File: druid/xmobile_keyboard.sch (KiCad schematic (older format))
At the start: 22 parts

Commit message: Added microSD slot.
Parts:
- removed R?: 10kOmh, Resistors_SMD:R_0603_HandSoldering, symbol R-RESCUE-xmobile
- added >0.1mk (x2): C, symbol C
- added D? (x4): LED, symbol LED
- added R? (x3): 10k, Resistors_SMD:R_0603_HandSoldering, symbol R-RESCUE-xmobile
- added R? (x4): 1k, Resistors_SMD:R_0603_HandSoldering, symbol R-RESCUE-xmobile
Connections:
- net labels added: INT, LED1, LED2, LED3, LED4, SCL, SDA
- wire segments 59 -> 77
- no-connect marks 7 -> 3
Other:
- note added: "Active low"

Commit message: Add xmega pcb, Add SIM800 pcb Add SRAM pcb, Start to draw sim card holder pcb
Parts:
- D? (x4): symbol LED -> LED-RESCUE-xmobile
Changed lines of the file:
@@
 Active low
 $Comp
-L LED D?
+L LED-RESCUE-xmobile D?
 U 1 1 5C4C2FCD
 P 2575 5400
@@
 	2575 5550 2575 5700
 $Comp
-L LED D?
+L LED-RESCUE-xmobile D?
 U 1 1 5C4C4192
 P 3050 5400
@@
 	3050 5550 3050 5700
 $Comp
-L LED D?
+L LED-RESCUE-xmobile D?
 U 1 1 5C4C43FA
 P 3450 5400
@@
 	3450 5550 3450 5700
 $Comp
-L LED D?
+L LED-RESCUE-xmobile D?
 U 1 1 5C4C4408
 P 3925 5400

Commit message: Old buttons replaced by membran buttons (electic and pcb) Added pcb for MAX7370 Cleared PCBs of resistor, capacitors and diodes
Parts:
- removed U? (x20): switch1, switch1:switch_6x9, symbol switch1
- added SW? (x20): SW_PUSH, druid:button_4pin_7,5x5, symbol SW_PUSH
- R? (x7): footprint Resistors_SMD:R_0603_HandSoldering -> (none)
- U?: footprint (none) -> druid:W252F2+1_21-0453

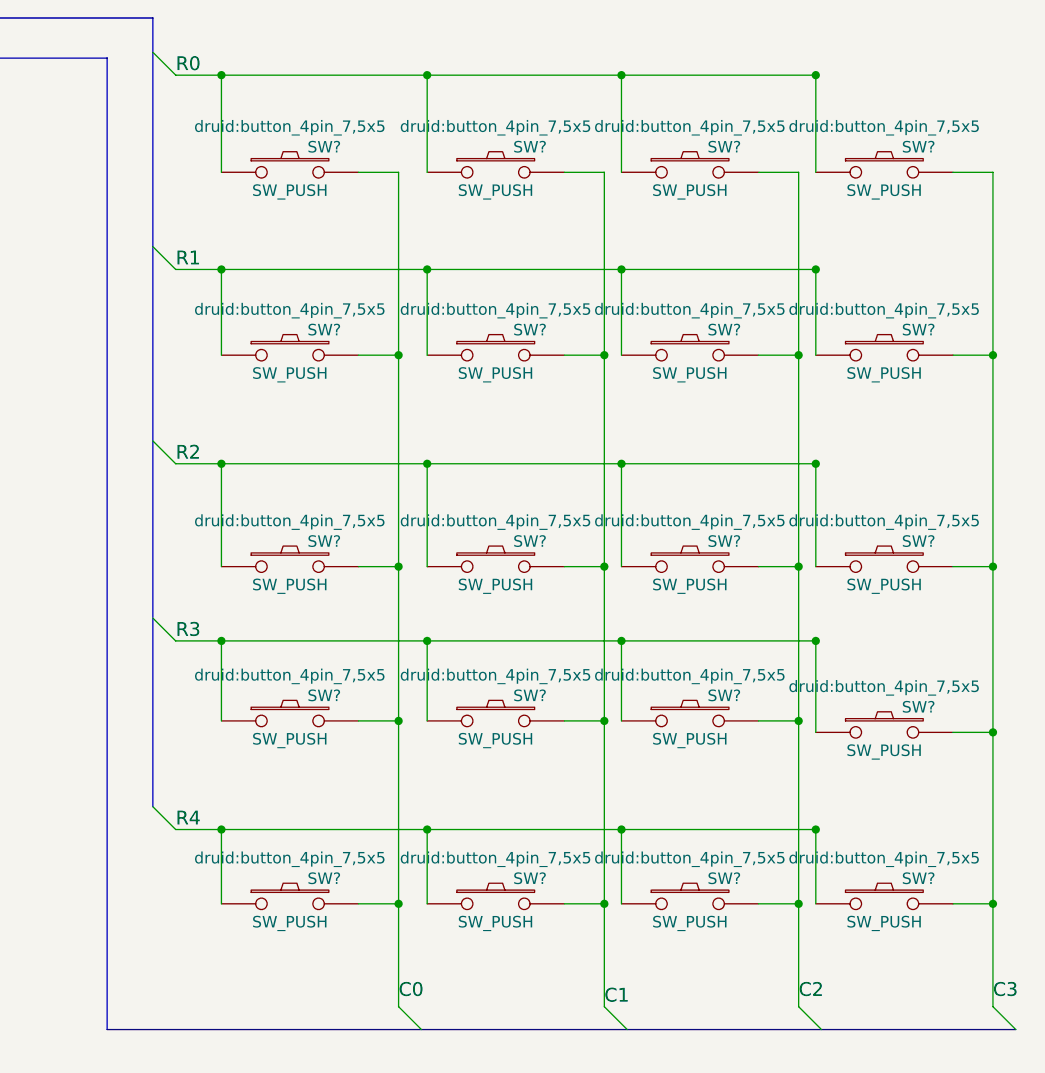
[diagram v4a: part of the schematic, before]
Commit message: Add some packages
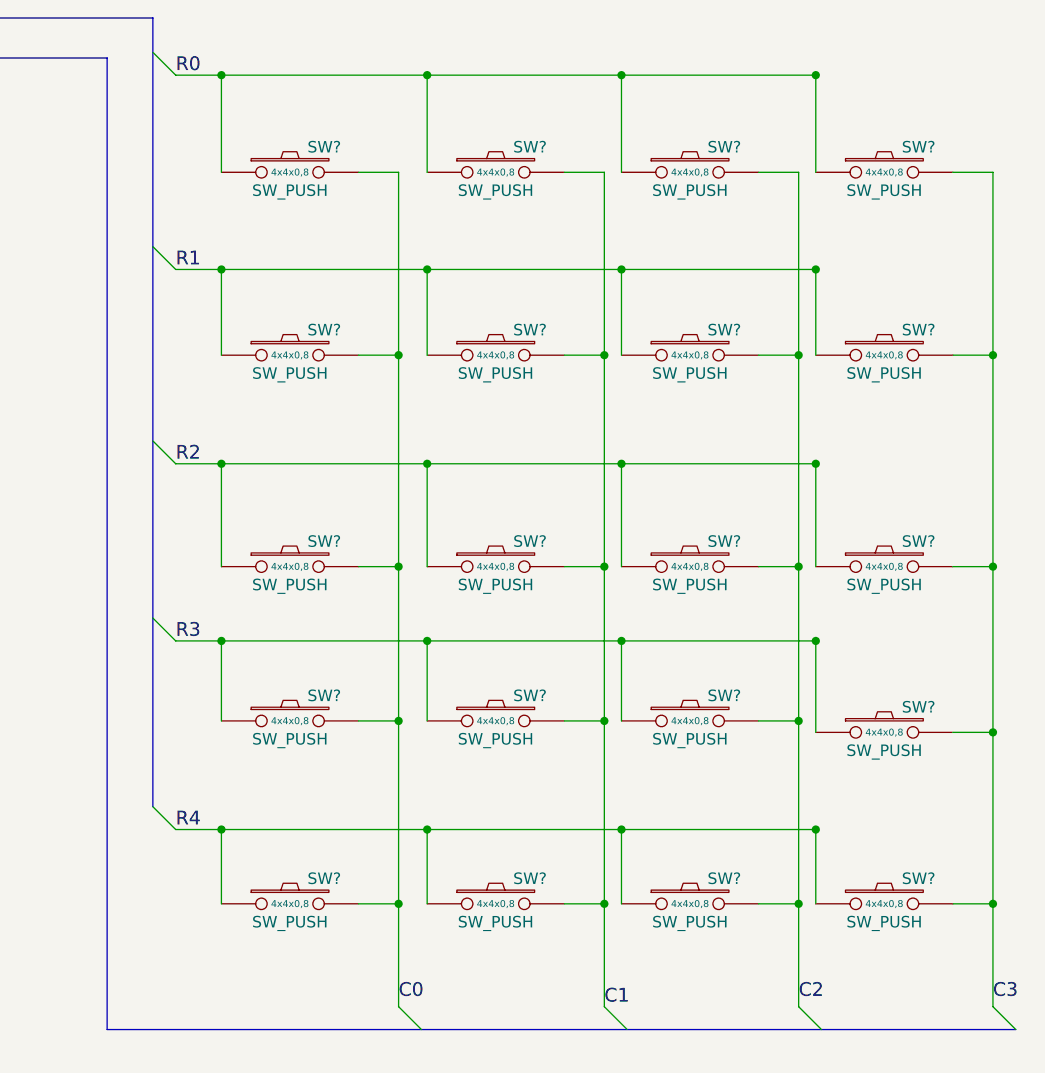
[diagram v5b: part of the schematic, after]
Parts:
- removed SW? (x19): SW_PUSH, druid:button_4pin_7,5x5, symbol SW_PUSH
- added SW? (x19): SW_PUSH, druid:button_4pin_7,5x5, symbol SW_PUSH
- SW?: case (none) -> 4x4x0,8; example (none) -> https://ru.aliexpress.com/item/100-4-4-0-8/32909011951.html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
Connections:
- net C0: now also SW?.2, SW?.2, SW?.2, SW?.2
- net C1: now also SW?.2, SW?.2, SW?.2, SW?.2, SW?.2
- net C2: now also SW?.2, SW?.2, SW?.2, SW?.2, SW?.2
- net C3: now also SW?.2, SW?.2, SW?.2, SW?.2, SW?.2
- net R0: now also SW?.1, SW?.1, SW?.1
- net R1: now also SW?.1, SW?.1, SW?.1, SW?.1
- net R2: now also SW?.1, SW?.1, SW?.1, SW?.1
- net R3: now also SW?.1, SW?.1, SW?.1, SW?.1
- net R4: now also SW?.1, SW?.1, SW?.1, SW?.1

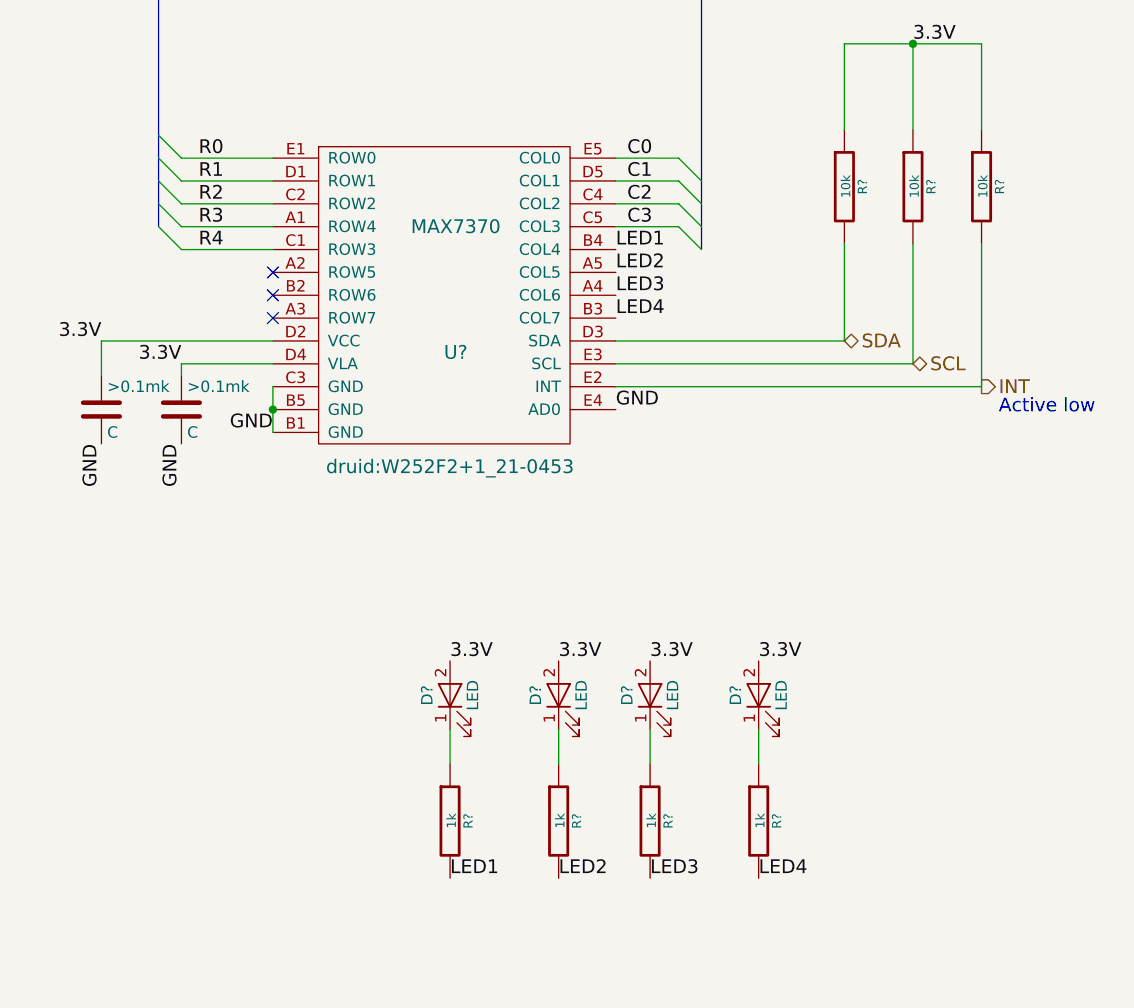
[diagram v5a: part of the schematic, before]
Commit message: Add packages: power module completed. Add packages: keyboard module completed.
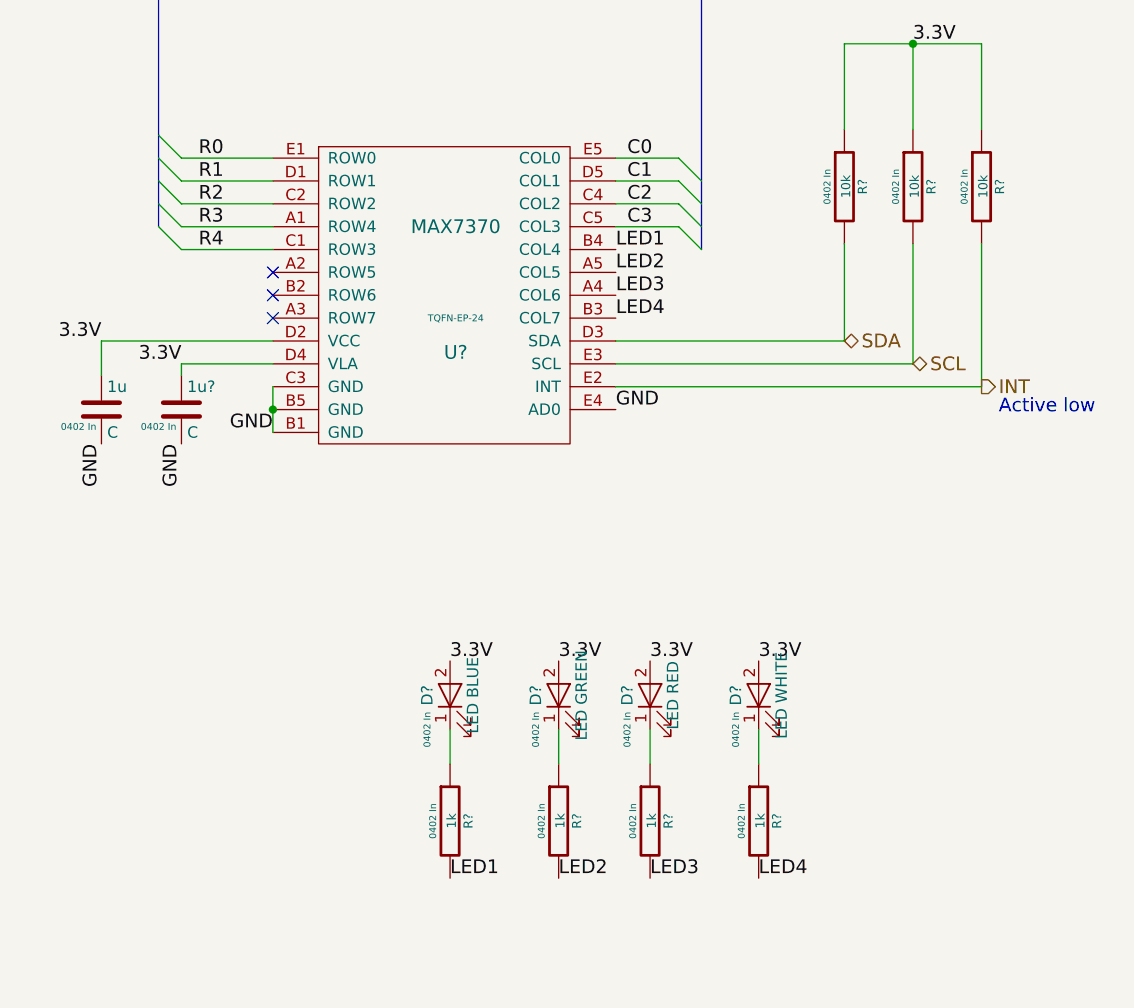
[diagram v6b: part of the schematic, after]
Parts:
- removed >0.1mk: C, symbol C
- removed R? (x2): 10k, symbol R-RESCUE-xmobile
- removed R? (x3): 1k, symbol R-RESCUE-xmobile
- added 1u?: C, Capacitors_SMD:C_0402, symbol C
- added R? (x3): 1k, Resistors_SMD:R_0402, symbol R-RESCUE-xmobile
- added R? (x2): 10k, Resistors_SMD:R_0402, symbol R-RESCUE-xmobile
- 1u: renamed from >0.1mk; footprint (none) -> Capacitors_SMD:C_0402; case (none) -> 0402 In; example (none) -> https://eu.mouser.com/ProductDetail/Murata-Electronics/GRM1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
- D?: value LED -> LED BLUE; footprint (none) -> LEDs_git:LED_0402; case (none) -> 0402 In; example (none) -> https://eu.mouser.com/ProductDetail/ROHM-Semiconductor/SMLP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
- D?: value LED -> LED GREEN; footprint (none) -> LEDs_git:LED_0402; case (none) -> 0402 In; example (none) -> https://eu.mouser.com/ProductDetail/ROHM-Semiconductor/SML-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
- D?: value LED -> LED RED; footprint (none) -> LEDs_git:LED_0402; case (none) -> 0402 In; example (none) -> https://eu.mouser.com/ProductDetail/ROHM-Semiconductor/SML-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
- D?: value LED -> LED WHITE; footprint (none) -> LEDs_git:LED_0402; case (none) -> 0402 In; example (none) -> https://eu.mouser.com/ProductDetail/OSRAM-Opto-Semiconducto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
- R?: footprint (none) -> Resistors_SMD:R_0402; case (none) -> 0402 In; example (none) -> https://eu.mouser.com/ProductDetail/ROHM-Semiconductor/SFR0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
- R?: footprint (none) -> Resistors_SMD:R_0402; case (none) -> 0402 In; example (none) -> https://eu.mouser.com/ProductDetail/Vishay/CRCW04021K00FKED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
- U?: case (none) -> TQFN-EP-24; example (none) -> https://eu.mouser.com/ProductDetail/Maxim-Integrated/MAX737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
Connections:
- net 3.3V: now also 1u?.1, R?.1, R?.1
- net GND: now also 1u?.2
- net INT: now also R?.2
- net LED2: now also R?.2
- net LED3: now also R?.2
- net LED4: now also R?.2
- net SCL: now also R?.2
- net at D?.1 (K): now also R?.1 (x3)

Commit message: move to kicad 5
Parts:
- 1u, 1u?: symbol C -> xmobile-rescue:C
- D? (x4): symbol LED-RESCUE-xmobile -> xmobile-rescue:LED-RESCUE-xmobile
- R? (x7): symbol R-RESCUE-xmobile -> xmobile-rescue:R-RESCUE-xmobile
- SW? (x20): symbol SW_PUSH -> xmobile-rescue:SW_PUSH
- U?: symbol MAX7370 -> xmobile-rescue:MAX7370
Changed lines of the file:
@@
-EESchema Schematic File Version 2
-LIBS:xmobile-rescue
-LIBS:power
-LIBS:device
-LIBS:transistors
-LIBS:conn
-LIBS:linear
-LIBS:regul
-LIBS:74xx
-LIBS:cmos4000
-LIBS:adc-dac
-LIBS:memory
-LIBS:xilinx
-LIBS:microcontrollers
-LIBS:dsp
-LIBS:microchip
-LIBS:analog_switches
-LIBS:motorola
-LIBS:texas
-LIBS:intel
-LIBS:audio
-LIBS:interface
-LIBS:digital-audio
-LIBS:philips
-LIBS:display
-LIBS:cypress
-LIBS:siliconi
-LIBS:opto
-LIBS:atmel
-LIBS:contrib
-LIBS:valves
-LIBS:XC6206P332MR
-LIBS:STF202-22T1G
-LIBS:MCP73871
-LIBS:switch1
-LIBS:SRAM
-LIBS:xmega128a1u_bga100
-LIBS:sim-holders
-LIBS:max7370
-LIBS:tp4056
+EESchema Schematic File Version 4
 LIBS:xmobile-cache
-EELAYER 25 0
+EELAYER 26 0
 EELAYER END
 $Descr A4 11693 8268
@@
 $EndDescr
 $Comp
-L MAX7370 U?
+L xmobile-rescue:MAX7370 U?
 U 1 1 5C4B05E9
 P 2600 3750
@@
 NoConn ~ 1800 3550
 $Comp
-L R-RESCUE-xmobile R?
+L xmobile-rescue:R-RESCUE-xmobile R?
 U 1 1 5C49881F
 P 4300 3175
@@
 INT
 $Comp
-L C 1u
+L xmobile-rescue:C 1u
 U 1 1 5C4C0F77
 P 1050 4150
@@
 Active low
 $Comp
-L LED-RESCUE-xmobile D?
+L xmobile-rescue:LED-RESCUE-xmobile D?
 U 1 1 5C4C2FCD
 P 2575 5400
@@
 3.3V
 $Comp
-L R-RESCUE-xmobile R?
+L xmobile-rescue:R-RESCUE-xmobile R?
 U 1 1 5C4C321E
 P 2575 5950
@@
 	2575 5550 2575 5700
 $Comp
-L LED-RESCUE-xmobile D?
+L xmobile-rescue:LED-RESCUE-xmobile D?
 U 1 1 5C4C4192
 P 3050 5400
@@
 	3050 5550 3050 5700
 $Comp
-L LED-RESCUE-xmobile D?
+L xmobile-rescue:LED-RESCUE-xmobile D?
 U 1 1 5C4C43FA
 P 3450 5400
@@
 	3450 5550 3450 5700
 $Comp
-L LED-RESCUE-xmobile D?
+L xmobile-rescue:LED-RESCUE-xmobile D?
 U 1 1 5C4C4408
 P 3925 5400
@@
 LED4
 $Comp
-L SW_PUSH SW?
+L xmobile-rescue:SW_PUSH SW?
 U 1 1 5C4FFA32
 P 6675 1975
@@
 	9750 1975 9750 5625
 $Comp
-L SW_PUSH SW?
+L xmobile-rescue:SW_PUSH SW?
 U 1 1 5C6DCE7B
 P 7575 1975
@@
 $EndComp
 $Comp
-L SW_PUSH SW?
+L xmobile-rescue:SW_PUSH SW?
 U 1 1 5C6DCF38
 P 8425 1975
@@
 $EndComp
 $Comp
-L SW_PUSH SW?
+L xmobile-rescue:SW_PUSH SW?
 U 1 1 5C6DD084
 P 6675 2775
@@
 $EndComp
 $Comp
-L SW_PUSH SW?
+L xmobile-rescue:SW_PUSH SW?
 U 1 1 5C6DD126
 P 7575 2775
@@
 $EndComp
 $Comp
-L SW_PUSH SW?
+L xmobile-rescue:SW_PUSH SW?
 U 1 1 5C6DD1D1
 P 8425 2775
@@
 $EndComp
 $Comp
-L SW_PUSH SW?
+L xmobile-rescue:SW_PUSH SW?
 U 1 1 5C6DD300
 P 9275 1975
@@
 $EndComp
 $Comp
-L SW_PUSH SW?
+L xmobile-rescue:SW_PUSH SW?
 U 1 1 5C6DD3BD
 P 9275 2775
@@
 $EndComp
 $Comp
-L SW_PUSH SW?
+L xmobile-rescue:SW_PUSH SW?
 U 1 1 5C6DD583
 P 6675 3700
@@
 $EndComp
 $Comp
-L SW_PUSH SW?
+L xmobile-rescue:SW_PUSH SW?
 U 1 1 5C6DD636
 P 6675 4375
@@
 $EndComp
 $Comp
-L SW_PUSH SW?
+L xmobile-rescue:SW_PUSH SW?
 U 1 1 5C6DD6E4
 P 7575 4375
@@
 $EndComp
 $Comp
-L SW_PUSH SW?
+L xmobile-rescue:SW_PUSH SW?
 U 1 1 5C6DD787
 P 7575 3700
@@
 $EndComp
 $Comp
-L SW_PUSH SW?
+L xmobile-rescue:SW_PUSH SW?
 U 1 1 5C6DD88C
 P 8425 3700
@@
 $EndComp
 $Comp
-L SW_PUSH SW?
+L xmobile-rescue:SW_PUSH SW?
 U 1 1 5C6DD941
 P 8425 4375
@@
 $EndComp
 $Comp
-L SW_PUSH SW?
+L xmobile-rescue:SW_PUSH SW?
 U 1 1 5C6DDA70
 P 9275 3700
@@
 $EndComp
 $Comp
-L SW_PUSH SW?
+L xmobile-rescue:SW_PUSH SW?
 U 1 1 5C6DDB57
 P 9275 4425
@@
 $EndComp
 $Comp
-L SW_PUSH SW?
+L xmobile-rescue:SW_PUSH SW?
 U 1 1 5C6DDCFE
 P 6675 5175
@@
 $EndComp
 $Comp
-L SW_PUSH SW?
+L xmobile-rescue:SW_PUSH SW?
 U 1 1 5C6DDDAF
 P 7575 5175
@@
 $EndComp
 $Comp
-L SW_PUSH SW?
+L xmobile-rescue:SW_PUSH SW?
 U 1 1 5C6DDEF8
 P 8425 5175
@@
 $EndComp
 $Comp
-L SW_PUSH SW?
+L xmobile-rescue:SW_PUSH SW?
 U 1 1 5C6DDFAF
 P 9275 5175
@@
 $EndComp
 $Comp
-L C 1u?
+L xmobile-rescue:C 1u?
 U 1 1 5C6E6190
 P 1400 4150
@@
 $EndComp
 $Comp
-L R-RESCUE-xmobile R?
+L xmobile-rescue:R-RESCUE-xmobile R?
 U 1 1 5C6E6DE1
 P 3050 5950
@@
 $EndComp
 $Comp
-L R-RESCUE-xmobile R?
+L xmobile-rescue:R-RESCUE-xmobile R?
 U 1 1 5C6E6E9E
 P 3450 5950
@@
 $EndComp
 $Comp
-L R-RESCUE-xmobile R?
+L xmobile-rescue:R-RESCUE-xmobile R?
 U 1 1 5C6E7B9A
 P 4600 3175
@@
 $EndComp
 $Comp
-L R-RESCUE-xmobile R?
+L xmobile-rescue:R-RESCUE-xmobile R?
 U 1 1 5C6E7C9E
 P 4900 3175
@@
 $EndComp
 $Comp
-L R-RESCUE-xmobile R?
+L xmobile-rescue:R-RESCUE-xmobile R?
 U 1 1 5C6E62AB
 P 3925 5950

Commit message: looks like all packages added.
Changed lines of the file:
@@
 Wire Wire Line
 	8975 1550 8975 1975
-Connection ~ 8975 1550
-Wire Wire Line
-	7150 1975 7150 5625
-Wire Wire Line
-	8050 1975 8050 5625
-Wire Wire Line
-	8900 1975 8900 5625
+Wire Wire Line
+	7150 1975 7150 2775
+Wire Wire Line
+	8050 1975 8050 2775
+Wire Wire Line
+	8900 1975 8900 2775
 Wire Wire Line
 	6375 2775 6375 2400
@@
 Wire Wire Line
 	8975 2400 8975 2775
-Connection ~ 8975 2400
 Wire Wire Line
 	8975 3250 8975 3700
-Connection ~ 8975 3250
 Wire Wire Line
 	6375 4375 6375 4025
@@
 Wire Wire Line
 	8975 4025 8975 4425
-Connection ~ 8975 4025
 Wire Wire Line
 	6375 5175 6375 4850
@@
 Wire Wire Line
 	8975 4850 8975 5175
-Connection ~ 8975 4850
-Wire Wire Line
-	6175 1550 8975 1550
-Wire Wire Line
-	6175 2400 8975 2400
-Wire Wire Line
-	6175 3250 8975 3250
-Wire Wire Line
-	6175 4025 8975 4025
-Wire Wire Line
-	6175 4850 8975 4850
-Wire Bus Line
-	6075 1300 6075 4750
+Wire Wire Line
+	6175 1550 6375 1550
+Wire Wire Line
+	6175 2400 6375 2400
+Wire Wire Line
+	6175 3250 6375 3250
+Wire Wire Line
+	6175 4025 6375 4025
+Wire Wire Line
+	6175 4850 6375 4850
 Wire Bus Line
 	1300 1300 6075 1300
@@
 Wire Wire Line
 	3300 3350 3575 3350
-Wire Bus Line
-	9850 5725 5875 5725
 Wire Bus Line
 	5875 5725 5875 1475
 Wire Bus Line
 	5875 1475 3675 1475
-Wire Bus Line
-	3675 1475 3675 3450
-Wire Bus Line
-	1300 1300 1300 3350
-Wire Wire Line
-	1800 4050 1800 4250
+Wire Wire Line
+	1800 4050 1800 4150
 Connection ~ 1800 4150
 Wire Wire Line
-	4300 2550 4900 2550
+	4300 2550 4600 2550
 Wire Wire Line
 	4300 2550 4300 2925
@@
 Connection ~ 9750 5175
 Wire Wire Line
-	9750 1975 9750 5625
+	9750 1975 9750 2775
 $Comp
 L xmobile-rescue:SW_PUSH SW?
@@
 	1    0    0    -1
 $EndComp
+Wire Wire Line
+	6375 1550 7275 1550
+Wire Wire Line
+	7275 1550 8125 1550
+Wire Wire Line
+	8125 1550 8975 1550
+Wire Wire Line
+	6375 2400 7275 2400
+Wire Wire Line
+	7275 2400 8125 2400
+Wire Wire Line
+	6375 3250 7275 3250
+Wire Wire Line
+	7275 3250 8125 3250
+Wire Wire Line
+	8125 3250 8975 3250
+Wire Wire Line
+	8125 2400 8975 2400
+Wire Wire Line
+	6375 4025 7275 4025
+Wire Wire Line
+	7275 4025 8125 4025
+Wire Wire Line
+	8125 4025 8975 4025
+Wire Wire Line
+	6375 4850 7275 4850
+Wire Wire Line
+	7275 4850 8125 4850
+Wire Wire Line
+	8125 4850 8975 4850
+Wire Wire Line
+	1800 4150 1800 4250
+Wire Wire Line
+	4600 2550 4900 2550
+Wire Wire Line
+	7150 3700 7150 4375
+Wire Wire Line
+	8050 3700 8050 4375
+Wire Wire Line
+	8900 3700 8900 4375
+Wire Wire Line
+	9750 3700 9750 4425
+Wire Wire Line
+	9750 2775 9750 3700
+Wire Wire Line
+	8900 2775 8900 3700
+Wire Wire Line
+	8050 2775 8050 3700
+Wire Wire Line
+	7150 2775 7150 3700
+Wire Wire Line
+	9750 4425 9750 5175
+Wire Wire Line
+	8900 4375 8900 5175
+Wire Wire Line
+	8050 4375 8050 5175
+Wire Wire Line
+	7150 4375 7150 5175
+Wire Wire Line
+	7150 5175 7150 5625
+Wire Wire Line
+	8050 5175 8050 5625
+Wire Wire Line
+	8900 5175 8900 5625
+Wire Wire Line
+	9750 5175 9750 5625
+Wire Bus Line
+	5875 5725 9850 5725
+Wire Bus Line
+	3675 1475 3675 3450
+Wire Bus Line
+	1300 1300 1300 3350
+Wire Bus Line
+	6075 1300 6075 4750
 $EndSCHEMATC
